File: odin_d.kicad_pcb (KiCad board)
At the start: 2 copper layers, 40.4 x 25 mm, 27 parts, among them J1 Conn_01x03, Q4 Q_NPN_BEC, Q5 Q_NPN_BEC, T1 BT136S

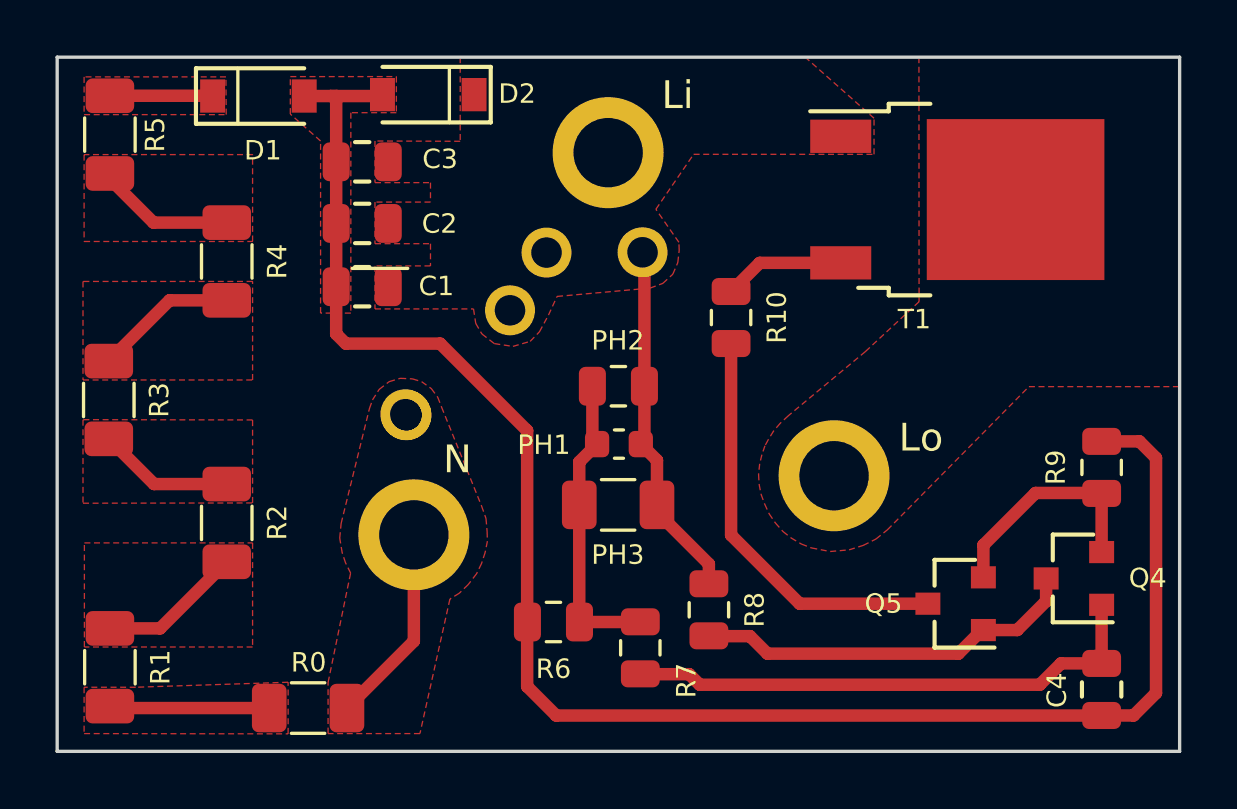
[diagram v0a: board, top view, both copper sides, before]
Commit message: Added 1210 footprint resistor for 110/220 VAC version
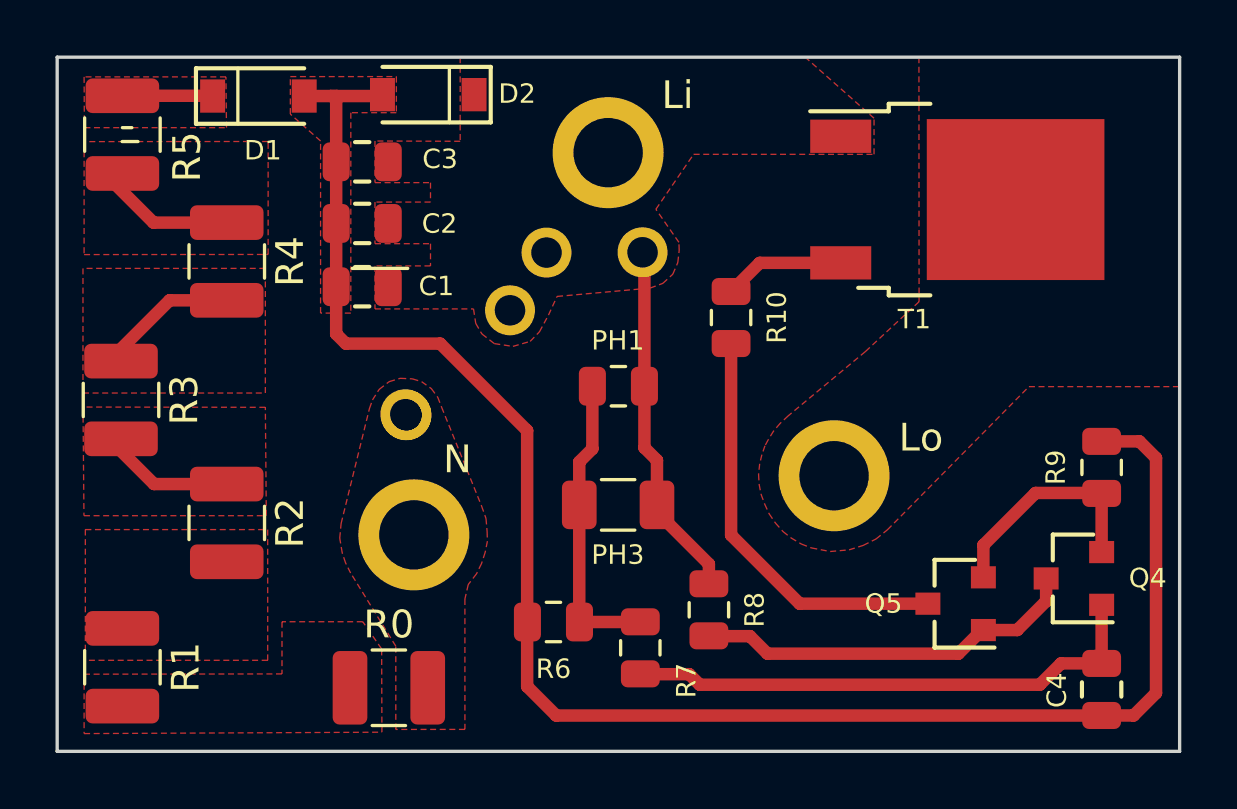
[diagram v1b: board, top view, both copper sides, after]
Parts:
- removed the PH1 at (150.8, 94.8)
- R0, R1, R2, R3, R4, R5: value 5.6k -> 3k; footprint Resistor_SMD:R_1206_3216Metric -> Resistor_SMD:R_1210_3225Metric
- moved R0 3.00 mm to (142.5, 103.6)
- moved R1 0.45 mm to (132.9, 102.9)
- moved R5 0.45 mm to (132.9, 83.7)
- moved R3 0.44 mm to (132.8, 93.2)
- renumbered PH2 to PH1
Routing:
- net /NEUTRAL: track 8.14 -> 0.00 mm
- net Net-(R0-Pad1): track 5.77 -> 0.00 mm
- net Net-(R1-Pad1): track 5.20 -> 0.00 mm

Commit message: Version compatible with fuse relay so the same stencial can be used for both
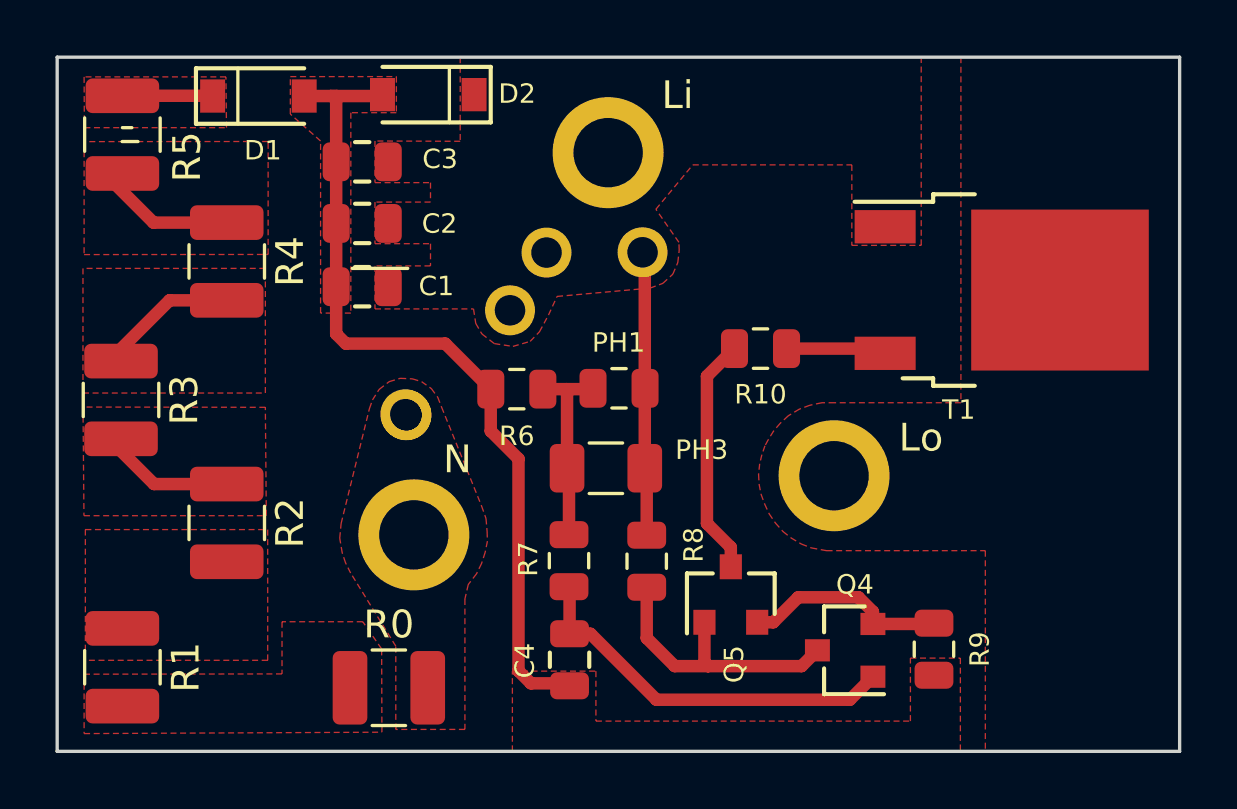
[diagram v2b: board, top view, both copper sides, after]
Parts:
- moved C4 19.2 mm to (149.0, 102.6)
- moved R9 8.91 mm to (162.1, 102.2), turned to 270 degrees
- moved Q4 8.64 mm to (158.9, 102.2)
- moved R6 8.49 mm to (147.1, 92.8)
- moved Q5 8.11 mm to (154.8, 100.2), turned to 90 degrees
- moved R7 4.06 mm to (149.0, 99.0)
- moved T1 3.63 mm to (164.6, 89.3)
- moved R8 2.84 mm to (151.8, 99.0)
- moved R10 1.54 mm to (155.9, 91.4), turned to 180 degrees
- moved PH3 1.39 mm to (150.3, 95.7)
- moved PH1 0.08 mm to (150.8, 92.8)
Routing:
- net /GND: track 63.5 -> 30.4 mm
- net Net-(Q5-Pad3): track 15.0 -> 8.63 mm
- net Net-(C4-Pad1): track 19.5 -> 14.0 mm
- net Net-(PH1-Pad1): track 11.1 -> 7.10 mm
- net Net-(Q4-Pad3): track 14.0 -> 10.3 mm
- net /LIVE: track 13.7 -> 11.4 mm
- net Net-(Q4-Pad2): track 8.32 -> 7.41 mm
- net Net-(R10-Pad1): track 4.38 -> 3.62 mm
